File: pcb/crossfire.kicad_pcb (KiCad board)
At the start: 4 copper layers, 100 x 49.8 mm, 110 parts, among them J1 USB-C, J2 SWD+UART, J3 USB_A, J4 USB_A, J5 USB_A, J6 USB_A, SW1 BOOT, SW2 RESET, SW3 USER, U1 USBLC6-2SC6, U10 TPS2065C, U11 USBLC6-2SC6, U12 TPS2065C, U13 USBLC6-2SC6, U2 W25Q128JVS, U3 RP2350A, U4 AP63203WU, U5 USB2514B, U6 TPS2065C, U7 USBLC6-2SC6, U8 TPS2065C, U9 USBLC6-2SC6, Y1 12MHz, Y2 24MHz

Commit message: final 0.1 pcb design
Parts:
- moved TP8 47.7 mm to (109.8, 54.5)
- moved TP4 34.7 mm to (129.9, 70.5)
- moved TP3 33.5 mm to (129.9, 72.8)
- moved U8 0.11 mm to (139.1, 80.7)
- moved U9 0.10 mm to (135.7, 80.7)
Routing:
- net /USB_D+: track 22.9 -> 23.9 mm
- net /port2/CONN_D+: track 3.81 -> 4.73 mm
- net /USB_D-: track 22.9 -> 23.8 mm
- net /port2/CONN_D-: track 5.23 -> 4.73 mm
- net Net-(J4-VBUS): track 12.7 -> 12.2 mm
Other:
- board text added: "+1.1V"
- board text added: "+3.3V"
- board text added: "+5V"
- board text added: "GND"
- board text added: "TP3"
- board text added: "TP4"
- board text removed: "3.3V"

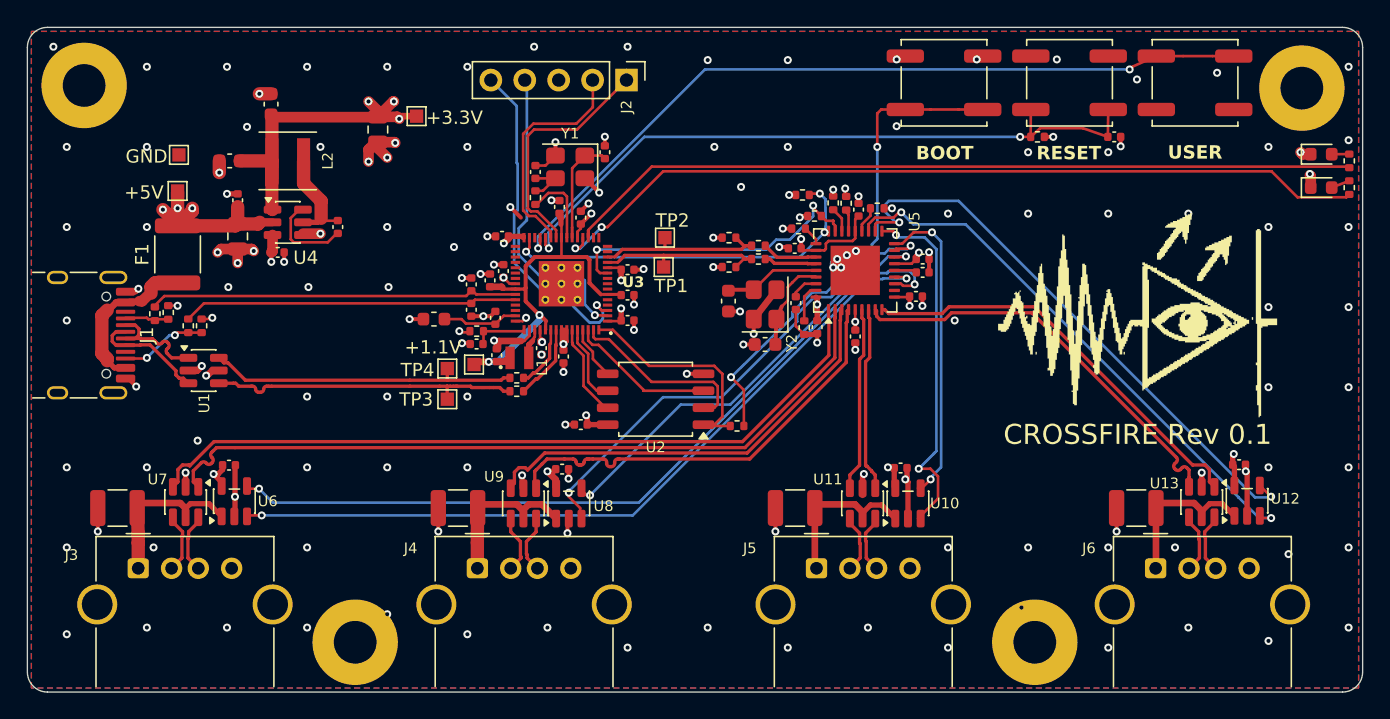
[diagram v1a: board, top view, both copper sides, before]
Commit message: fix silkscreen for final 0.1 pcb
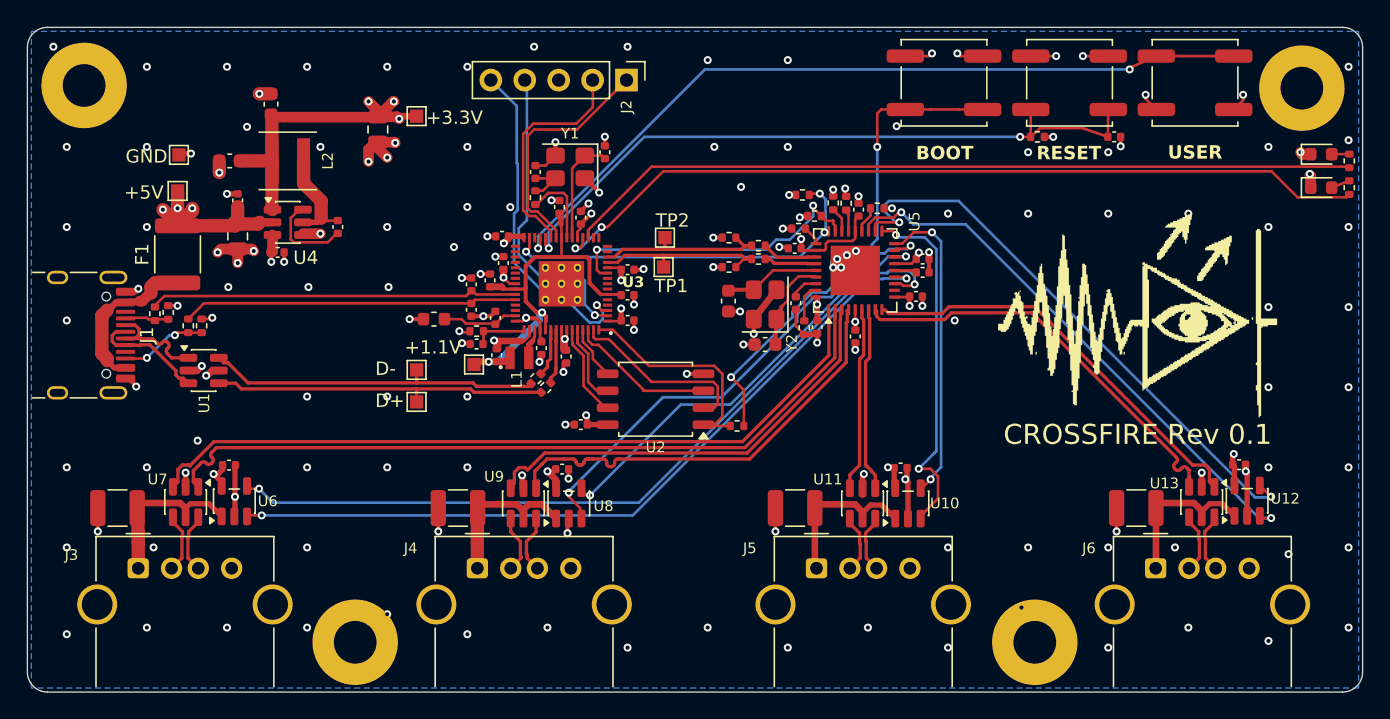
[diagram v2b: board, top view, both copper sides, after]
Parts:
- moved TP3 2.31 mm to (127.7, 73.0)
- moved TP4 2.30 mm to (127.7, 70.7)
- moved R22 2.20 mm to (137.3, 72.0), turned to 45 degrees
- moved R21 1.44 mm to (136.6, 71.3), turned to 45 degrees
- moved C8 0.60 mm to (134.2, 62.6)
- moved C7 0.20 mm to (138.8, 69.7)
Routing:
- net GND: track 86.7 -> 97.8 mm, vias 160 -> 162
- net +3V3: track 62.0 -> 64.2 mm, vias 20 -> 19
- net /USB_D-: track 23.8 -> 25.7 mm
- net /USB_D+: track 23.9 -> 25.8 mm
- net /mcu/MCU_D+: track 5.68 -> 4.13 mm
- net /mcu/MCU_D-: track 4.73 -> 3.61 mm
- removed copper zone on F.Cu, net GND
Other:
- board text added: "D+"
- board text added: "D-"
- board text removed: "TP3"
- board text removed: "TP4"
